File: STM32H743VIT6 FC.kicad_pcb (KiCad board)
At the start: 4 copper layers, 37 x 37 mm, 89 parts, among them J1 USB4730-GF-A, SW2 Y78B22310FP, U1 TPS54302DDCR, U2 USBLC6-2SC6, U3 TPS54302DDCR

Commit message: muha
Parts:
- added G***: LOGO, LOGO, B.Cu at (164.6, 121.0)

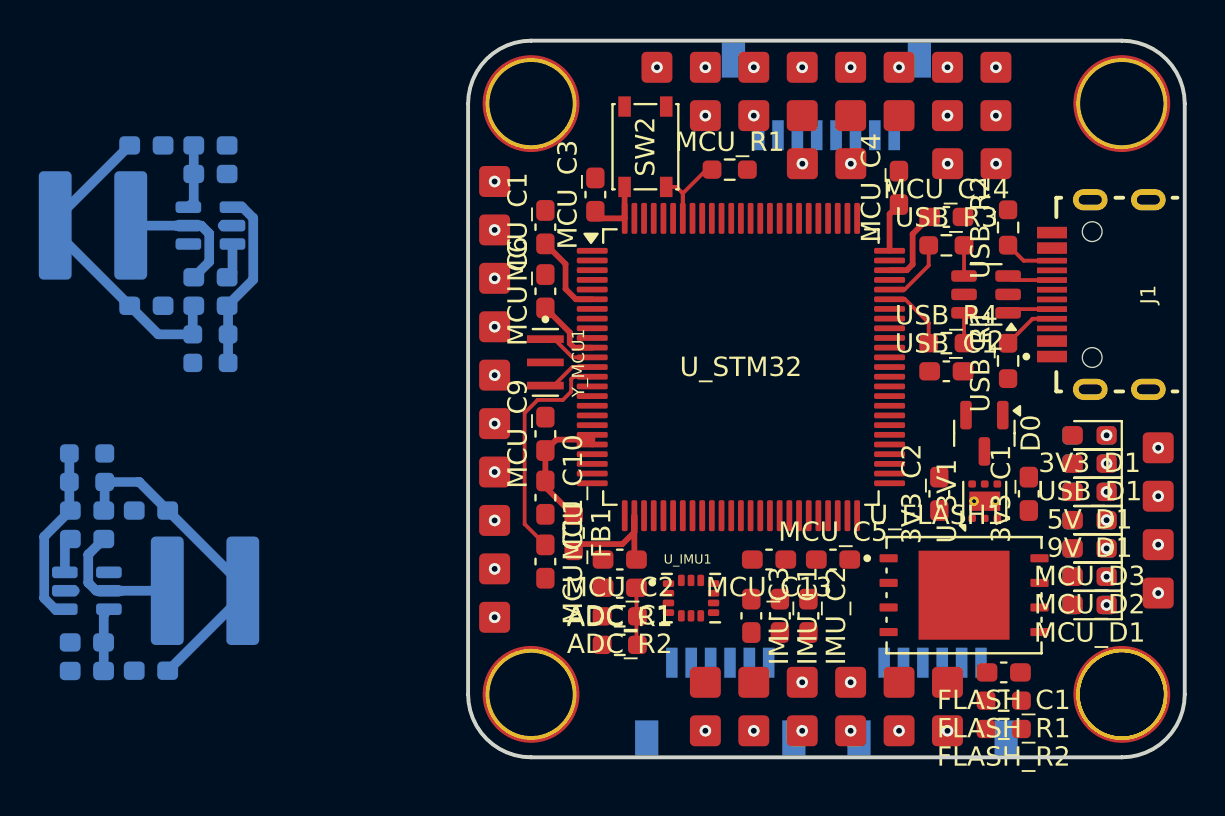
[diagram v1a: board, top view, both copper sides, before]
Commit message: Placed voltage regs and wired motors, gyro, and flash.
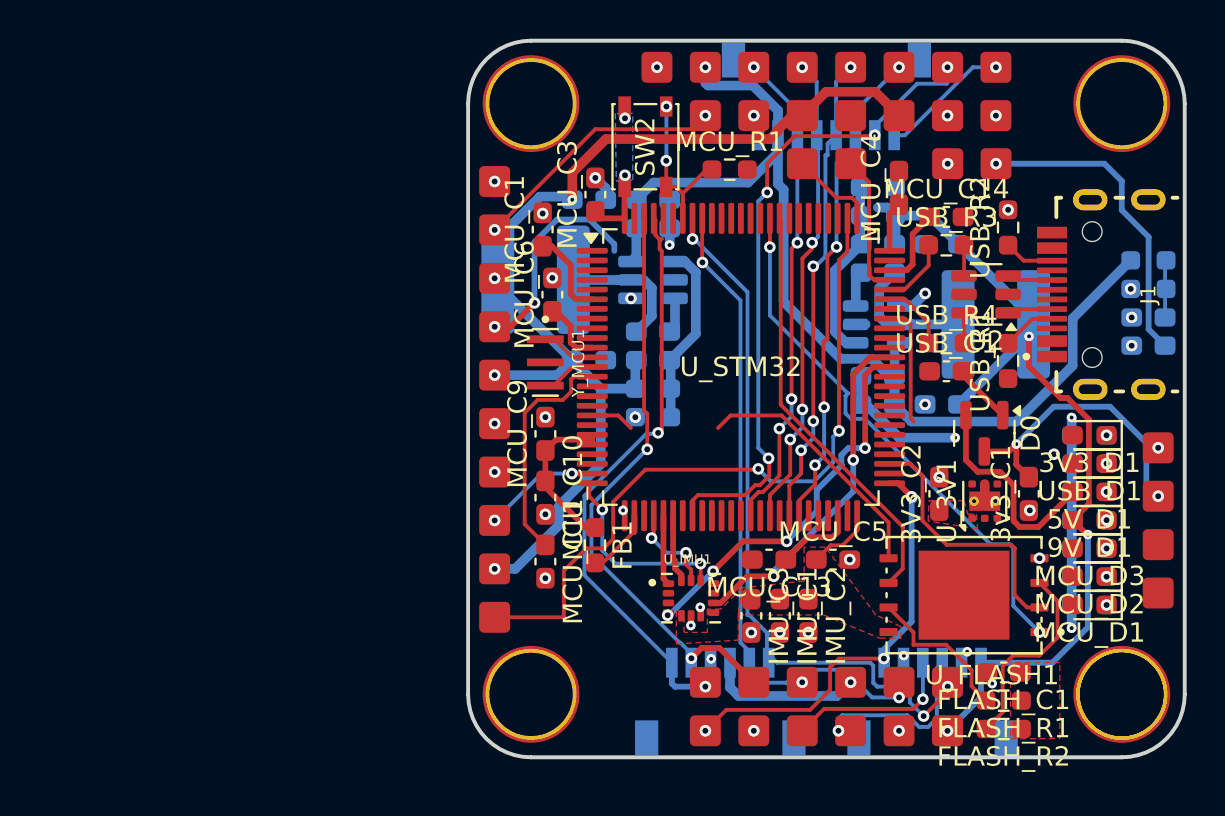
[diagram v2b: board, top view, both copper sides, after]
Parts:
- ADC_C1, ADC_R1, ADC_R2, MCU_C2: moved to B.Cu
- moved 9V_C12 43.1 mm to (168.4, 112.3)
- moved 9V_C9 43.1 mm to (168.4, 113.7)
- moved 9V_R7 43.1 mm to (168.4, 110.8)
- moved 9V_R8 43.1 mm to (168.4, 109.3)
- moved 9V_C7 43.1 mm to (168.4, 120.5)
- moved U3 43.1 mm to (168.4, 116.4)
- moved 9V_C8 43.1 mm to (168.4, 119.1)
- moved 9V_C10 43.1 mm to (171.7, 112.3)
- moved 9V_C11 43.1 mm to (171.7, 120.5)
- moved 9V_L1 43.1 mm to (174.5, 116.4)
- moved ADC_R1 33.7 mm to (182.4, 113.1)
- moved ADC_R2 32.1 mm to (182.4, 114.6)
- moved ADC_C1 30.7 mm to (182.4, 116.0)
- moved MCU_C2 29.4 mm to (182.4, 117.5)
- moved 5V_C12 23.0 mm to (156.8, 118.2)
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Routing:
- net BAT: track 6.61 -> 57.0 mm
- net 5V_REG: track 17.8 -> 67.7 mm, vias 2 -> 3
- net BEEPER: track 0.00 -> 36.7 mm, vias 1 -> 2
- net I2C1_SDA: track 0.00 -> 36.7 mm, vias 0 -> 3
- net I2C1_SCL: track 0.00 -> 35.1 mm, vias 0 -> 2
- net ADC_CURR: track 0.00 -> 33.9 mm, vias 1 -> 4
- net UART8_TX: track 0.00 -> 30.5 mm, vias 0 -> 2
- net UART8_RX: track 0.00 -> 30.2 mm, vias 0 -> 2
- net 9V_REG: track 17.8 -> 47.6 mm, vias 2 -> 4
- net SPI2_NSS: track 0.00 -> 28.2 mm, vias 0 -> 2
- net GND: track 0.00 -> 27.3 mm, vias 9 -> 41
- net MOTOR4: track 0.00 -> 25.4 mm, vias 1 -> 4
- net MOTOR1: track 0.00 -> 25.2 mm, vias 1 -> 4
- net MOTOR3: track 0.00 -> 24.6 mm, vias 1 -> 4
- net MOTOR2: track 0.00 -> 24.5 mm, vias 1 -> 4
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- added copper zone on B.Cu, net 3.3V
- added copper zone on F.Cu, net 3.3V

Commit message: layout
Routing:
- net 5V_USB: track 3.11 -> 28.6 mm
- net LED0: track 0.04 -> 15.3 mm
- net LED2: track 0.00 -> 14.4 mm, vias 0 -> 2
- net LED1: track 0.00 -> 14.1 mm, vias 0 -> 2
- net UART4_RX: track 11.2 -> 0.05 mm, vias 2 -> 1
- net UART1_TX: track 6.29 -> 0.00 mm
- net SPI2_MOSI: track 15.5 -> 21.6 mm
- net 3.3V: track 39.1 -> 44.6 mm
- net 5V_REG: track 67.7 -> 63.9 mm
- net 9V_REG: track 47.6 -> 44.1 mm
- net 5V: track 23.1 -> 20.4 mm
- net GND: track 27.3 -> 25.2 mm, vias 41 -> 42
- net UART5_RX: track 22.2 -> 20.8 mm
- net SPI2_NSS: track 28.2 -> 27.1 mm
- net BEEPER: track 36.7 -> 35.9 mm, vias 2 -> 3

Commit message: more
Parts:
- turned FLASH_C1 to 0 degrees
- turned FLASH_R1 to 0 degrees
- turned FLASH_R2 to 0 degrees
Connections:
- AVTX_J2 pad 1: 9V_REG -> 3.3V
- U_FLASH1 pad 9: (no net) -> GND
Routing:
- net 3.3V: track 44.6 -> 90.3 mm, vias 3 -> 4
- net Net-(U_FLASH1-/WP(IO2)): track 10.4 -> 0.00 mm
- net 5V: track 20.4 -> 26.7 mm
- net Net-(U_FLASH1-/HOLD(IO3)): track 7.88 -> 10.0 mm
- net GND: track 25.2 -> 27.0 mm, vias 42 -> 46
- net CAM: track 13.7 -> 14.9 mm
- net 5V_USB: track 28.6 -> 29.3 mm
- net 9V_REG: track 44.1 -> 44.3 mm, vias 4 -> 3
- net UART4_TX: vias 1 -> 0
- net UART4_RX: vias 1 -> 0
- removed copper zone on B.Cu, net 3.3V

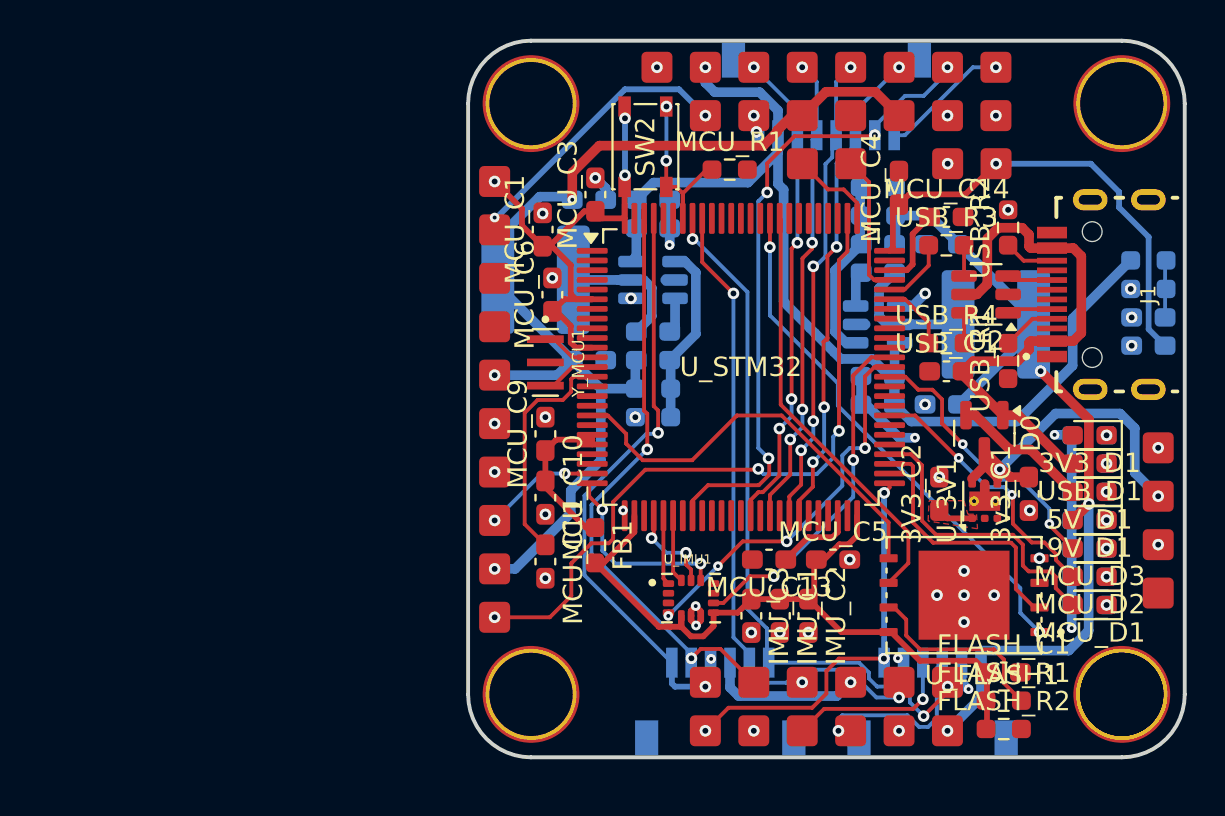
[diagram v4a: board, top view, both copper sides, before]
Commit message: Moved 5V regulator.
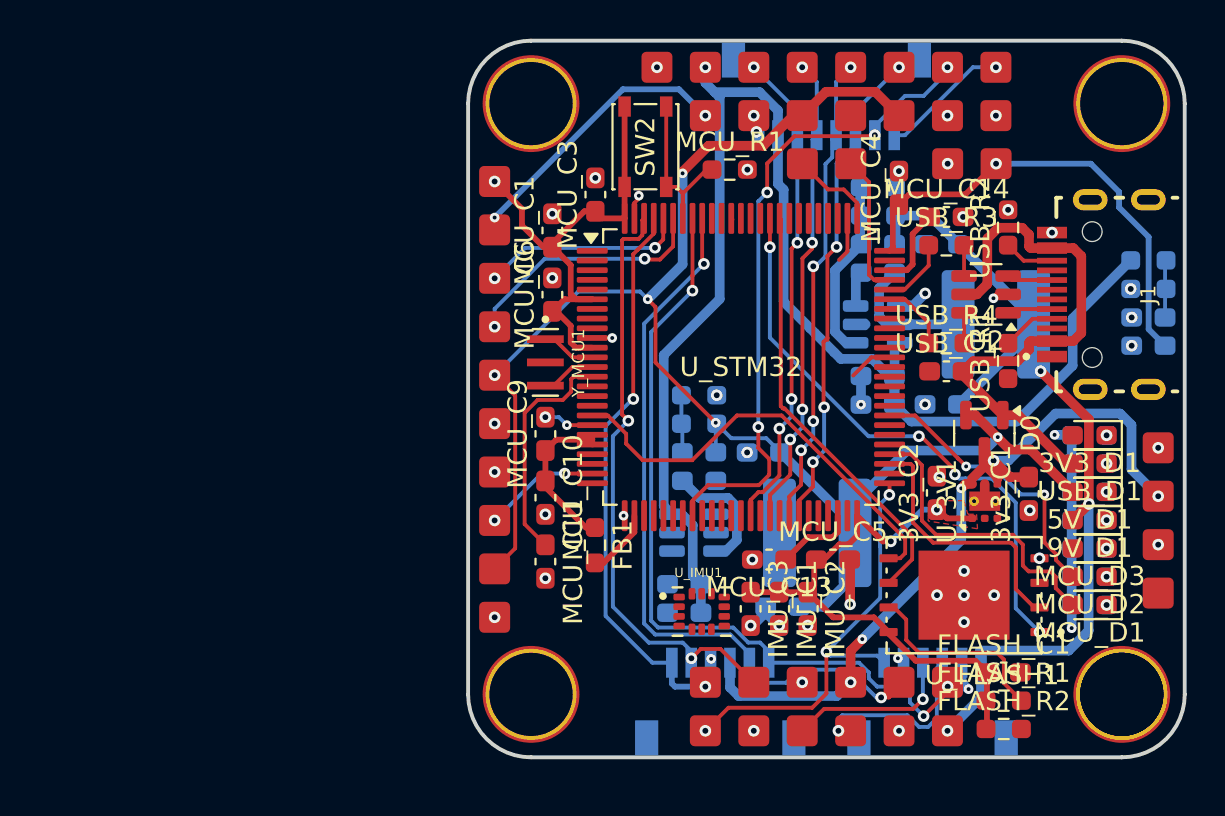
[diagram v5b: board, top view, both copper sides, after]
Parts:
- moved 5V_C11 23.3 mm to (163.5, 131.0), turned to 180 degrees
- moved 5V_C7 21.4 mm to (158.4, 131.3), turned to 180 degrees
- moved 5V_L1 19.6 mm to (165.3, 127.2), turned to 0 degrees
- moved 5V_C8 18.4 mm to (158.4, 129.8), turned to 180 degrees
- moved U1 13.2 mm to (158.9, 127.2)
- moved 5V_C10 10.2 mm to (162.5, 123.0), turned to 180 degrees
- moved 5V_C9 8.06 mm to (159.2, 124.5), turned to 0 degrees
- moved 5V_C12 5.32 mm to (159.2, 123.0), turned to 180 degrees
- moved 5V_R7 2.99 mm to (159.2, 121.5), turned to 180 degrees
- moved 5V_R8 2.63 mm to (159.2, 120.1), turned to 0 degrees
- moved U_IMU1 0.89 mm to (159.3, 131.2)
- moved MCU_C1 0.50 mm to (151.6, 111.5)
- moved IMU_C2 0.36 mm to (164.8, 131.1)
- moved IMU_C3 0.36 mm to (161.8, 131.1)
- moved IMU_C1 0.36 mm to (163.3, 131.1)
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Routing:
- net BEEPER: track 35.9 -> 2.32 mm, vias 3 -> 1
- net 5V_REG: track 63.9 -> 83.8 mm, vias 3 -> 5
- net GYRO_INT1: track 19.8 -> 0.00 mm, vias 4 -> 0
- net BAT: track 57.0 -> 73.8 mm
- net GYRO_CLKIN: track 18.0 -> 2.27 mm, vias 2 -> 0
- net LED2: track 14.4 -> 0.00 mm, vias 2 -> 0
- net 5V: track 26.7 -> 39.8 mm, vias 3 -> 5
- net UART4_RX: track 0.05 -> 13.0 mm, vias 0 -> 2
- net UART4_TX: track 0.00 -> 10.6 mm, vias 0 -> 2
- net GYRO_CS: track 9.82 -> 0.00 mm, vias 2 -> 0
- net Net-(U1-SW): track 7.47 -> 0.01 mm
- net 3.3V: track 90.3 -> 83.3 mm
- net Net-(U1-FB): track 9.36 -> 2.97 mm
- net I2C1_SCL: track 35.0 -> 40.7 mm
- net GYRO_SCK: track 4.74 -> 0.00 mm, vias 2 -> 0
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
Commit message: molec
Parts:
- moved G*** 10.6 mm to (156.6, 113.9)

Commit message: green
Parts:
- moved U_IMU1 1.77 mm to (157.7, 130.5)
- moved 5V_C7 1.74 mm to (160.1, 131.3), turned to 0 degrees
- moved 5V_C8 1.74 mm to (160.1, 129.8), turned to 0 degrees
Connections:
- AVTX_J2 pad 1: 3.3V -> BEEPER
- OTHER_J2 pad 1: BEEPER -> 3.3V
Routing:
- net GYRO_INT1: track 0.00 -> 23.2 mm, vias 0 -> 2
- net GYRO_CLKIN: track 2.27 -> 18.2 mm, vias 0 -> 2
- net UART2_TX: track 0.00 -> 15.8 mm
- net GND: track 28.4 -> 42.4 mm, vias 52 -> 56
- net UART2_RX: track 0.00 -> 13.9 mm
- net Net-(U_FLASH1-/WP(IO2)): track 0.00 -> 8.70 mm
- net GYRO_CS: track 0.00 -> 7.46 mm, vias 0 -> 2
- net GYRO_SCK: track 0.00 -> 6.12 mm, vias 0 -> 2
- net BAT: track 73.8 -> 68.8 mm
- net ADC_CURR: track 33.6 -> 29.2 mm
- net BOOT0: track 9.75 -> 5.60 mm
- net 3.3V: track 83.3 -> 87.3 mm
- net GYRO_MISO: track 0.00 -> 3.81 mm
- net GYRO_MOSI: track 0.00 -> 3.58 mm
- net BEEPER: track 2.32 -> 5.14 mm
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
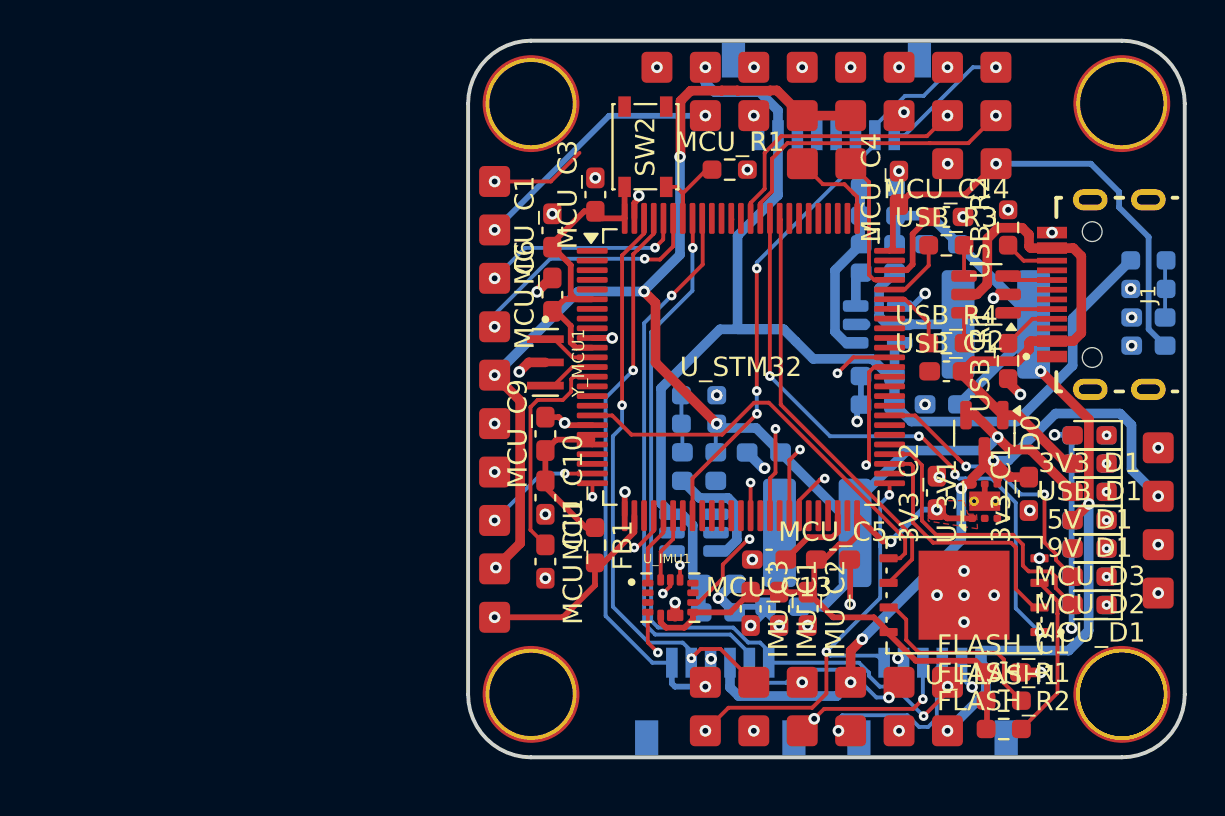
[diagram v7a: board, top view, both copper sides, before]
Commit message: Moved voltage divider back and wired uarts.
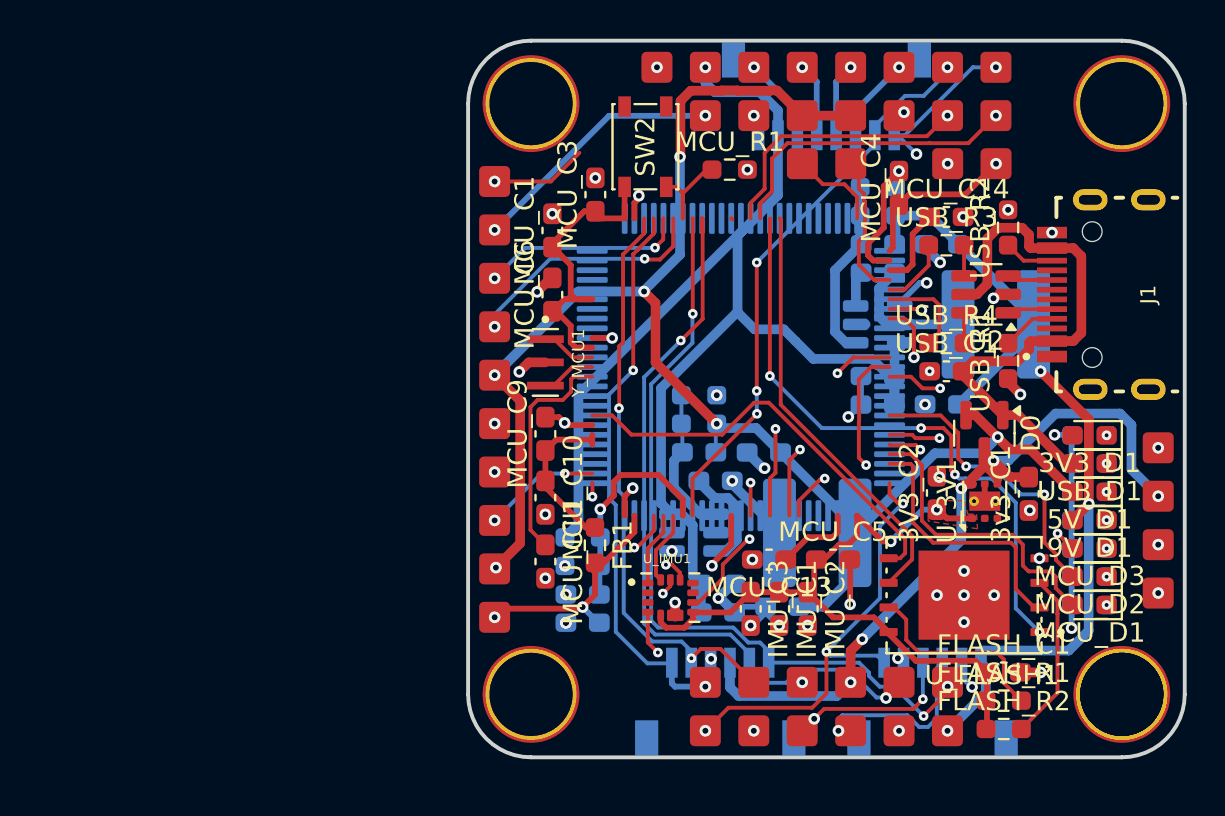
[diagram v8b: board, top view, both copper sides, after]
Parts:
- U_STM32: moved to B.Cu
- moved ADC_C1 32.5 mm to (153.2, 130.3)
- moved ADC_R1 32.5 mm to (153.2, 127.4)
- moved ADC_R2 32.5 mm to (153.2, 128.9)
- moved MCU_C2 32.5 mm to (153.2, 131.8)
- moved 5V_C9 0.85 mm to (160.0, 124.5)
- turned U_STM32 to 180 degrees
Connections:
- U_FLASH1 pad 9: GND -> (no net)
- U_STM32 pad 89: PINIO1 -> unconnected-(U_STM32-PB3-Pad89)
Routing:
- net UART7_RX: track 6.70 -> 38.7 mm, vias 1 -> 3
- net UART1_TX: track 0.00 -> 21.7 mm, vias 1 -> 2
- net UART1_RX: track 0.00 -> 19.8 mm, vias 1 -> 2
- net UART3_TX: track 9.81 -> 27.8 mm, vias 1 -> 2
- net UART3_RX: track 8.79 -> 25.3 mm, vias 2 -> 3
- net LED2: track 0.00 -> 14.8 mm, vias 0 -> 2
- net 3.3V: track 87.3 -> 72.7 mm, vias 4 -> 5
- net ADC_VBAT: track 2.97 -> 11.2 mm, vias 0 -> 1
- net GND: track 42.4 -> 49.5 mm, vias 56 -> 59
- net Net-(U1-FB): track 2.97 -> 7.73 mm
- net MOTOR4: track 25.4 -> 29.8 mm
- net MOTOR1: track 23.8 -> 28.3 mm
- net MOTOR3: track 24.5 -> 28.3 mm
- net MOTOR2: track 23.8 -> 27.7 mm
- net Net-(U1-SW): track 0.01 -> 3.71 mm, vias 0 -> 1
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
